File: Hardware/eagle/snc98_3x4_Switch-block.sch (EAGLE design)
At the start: 52 parts

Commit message: Switch-block changed Rev.02
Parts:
- D1, D10, D11, D12, D13, D14, D15, D2, D29, D3, D4, D5: device BaseApp:DIODESMA -> BaseApp:DIODESMA-WIDE
- H1, H10, H2, H3, H4, H5, H6, H7, H8, H9: value MOUNT-PAD-ROUND2.5 -> MOUNT-PAD-ROUND2.8; device holes:MOUNT-PAD-ROUND2.5 -> holes:MOUNT-PAD-ROUND2.8
- JP1: value M09LOCK-LONGPADS -> (none)
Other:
- note added: "0.2"
- note added: "snc98 3x4 Switch-block Rev. 0.2 by Jens Grabner is licensed under"
- note removed: "0.1"
- note removed: "snc98 3x4 Switch-block Rev. 0.1 by Jens Grabner is licensed under"
- moved on the sheet: D16, D17, D18, D19, D20, D21, H1, H10, H2, H3, H4, H5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

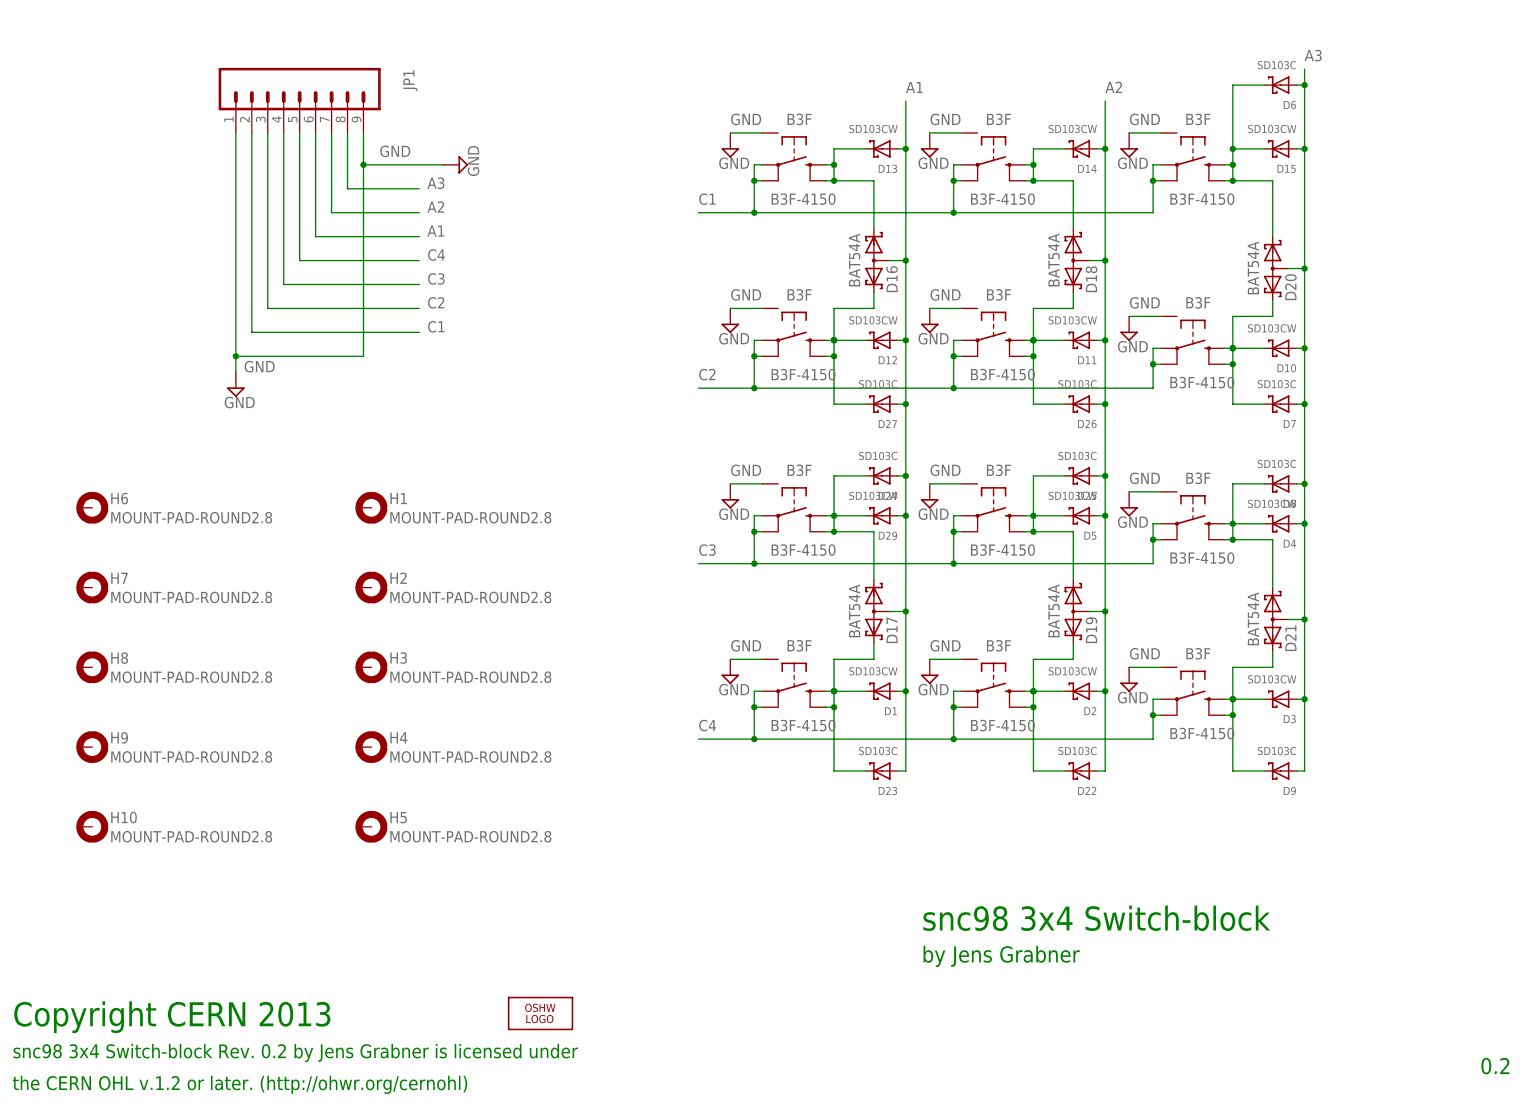
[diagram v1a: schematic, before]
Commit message: Switch-block Filter added
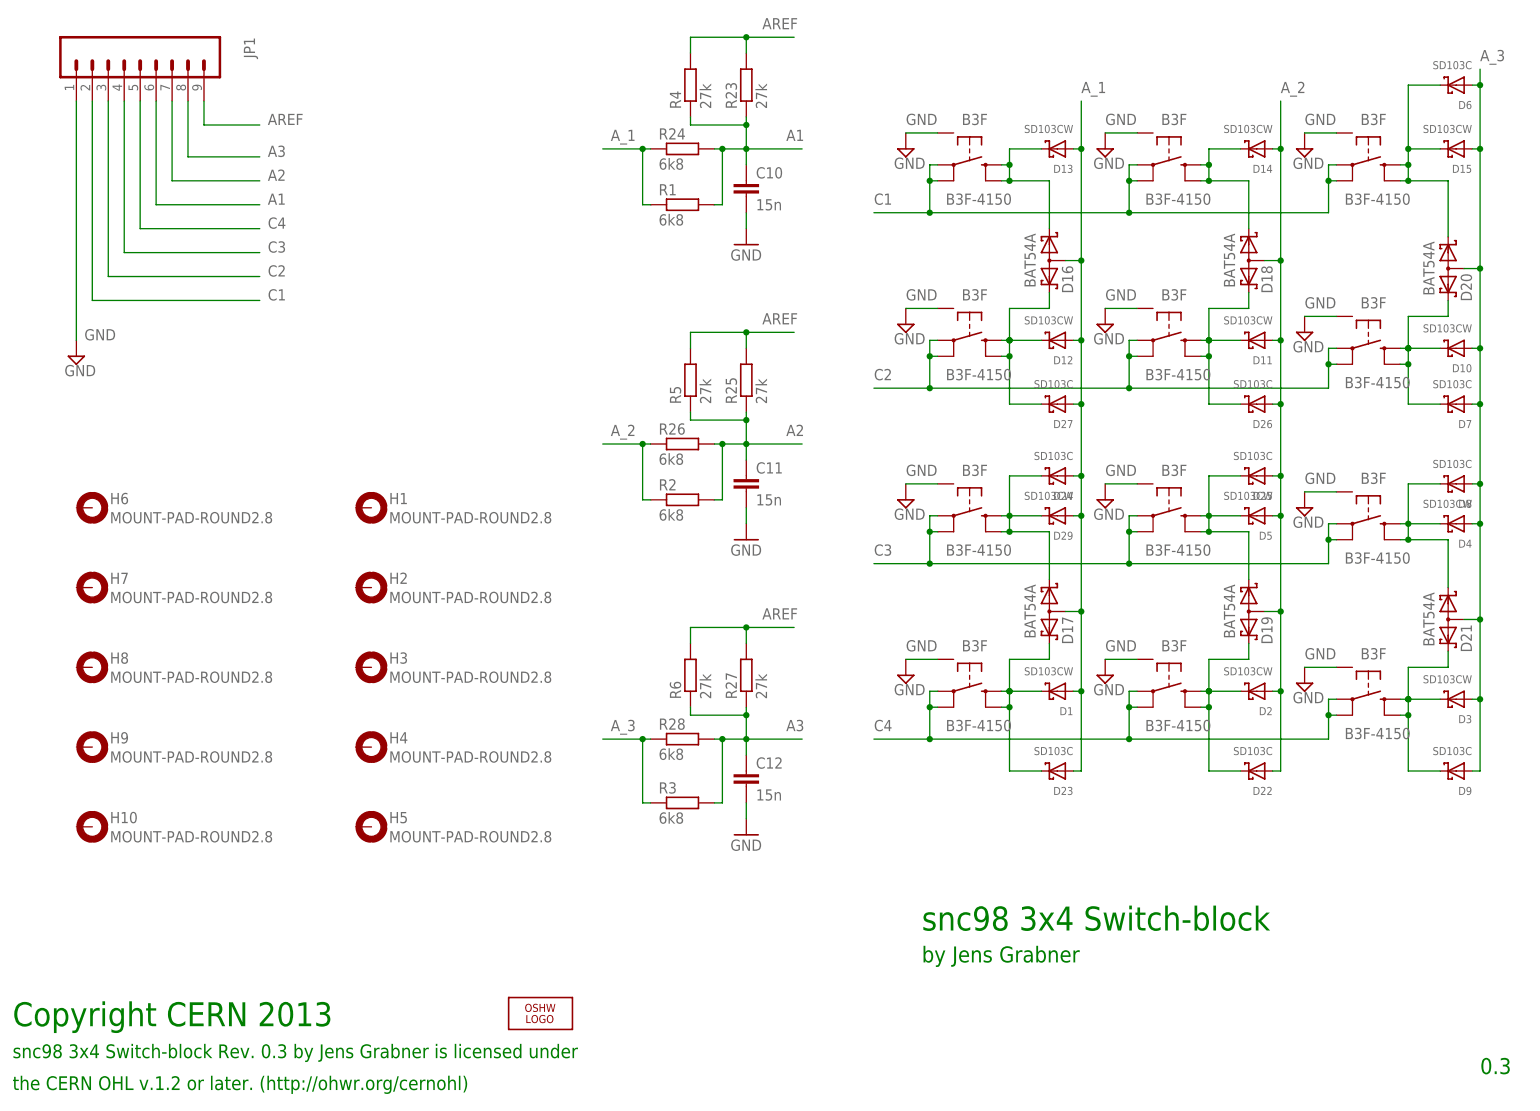
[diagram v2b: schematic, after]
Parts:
- added C10, C11, C12: 15n, rcl:C-EUC1206K
- added R1, R2, R3: 6k8, rcl:R-EU_R1206
- added R23, R25, R27: 27k, rcl:R-EU_0204/5
- added R24, R26, R28: 6k8, rcl:R-EU_0204/5
- added R4, R5, R6: 27k, rcl:R-EU_R1206
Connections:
- new net AREF: JP1.9, R23.2, R25.2, R27.2, R4.2, R5.2, R6.2
- new net A_1: D1.A, D12.A, D13.A, D16.AA, D17.AA, D23.A, D24.A, D27.A, D29.A, R1.1, R24.1
- new net A_2: D11.A, D14.A, D18.AA, D19.AA, D2.A, D22.A, D25.A, D26.A, D5.A, R2.1, R26.1
- new net A_3: D10.A, D15.A, D20.AA, D21.AA, D3.A, D4.A, D6.A, D7.A, D8.A, D9.A, R28.1, R3.1
- net A1: now also C10.1, R1.2, R23.1, R24.2, R4.1; no longer D1.A, D12.A, D13.A, D16.AA, D17.AA, D23.A, D24.A, D27.A, D29.A
- net A2: now also C11.1, R2.2, R25.1, R26.2, R5.1; no longer D11.A, D14.A, D18.AA, D19.AA, D2.A, D22.A, D25.A, D26.A, D5.A
- net A3: now also C12.1, R27.1, R28.2, R3.2, R6.1; no longer D10.A, D15.A, D20.AA, D21.AA, D3.A, D4.A, D6.A, D7.A, D8.A, D9.A
- net GND: now also C10.2, C11.2, C12.2; no longer JP1.9
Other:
- note added: "0.3"
- note added: "snc98 3x4 Switch-block Rev. 0.3 by Jens Grabner is licensed under"
- note removed: "0.2"
- note removed: "snc98 3x4 Switch-block Rev. 0.2 by Jens Grabner is licensed under"
- moved on the sheet: D1, D10, D11, D12, D13, D14, D15, D16, D17, D18, D19, D2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
